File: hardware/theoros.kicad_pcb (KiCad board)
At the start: 4 copper layers, 60 x 120 mm, 87 parts, among them J201 TYPE-C-31-M-12, J301 TC2030-NL, J401 U.FL, J501 DM3AT-SF-PEJM5, J502 FH12-30S-0.5SH(55), SW301 RESET, SW302 BOOT, SW303 EJECT, U201 USBLC6-2SC6, U202 AP7361C-33E, U301 ESP32-S3-WROOM-1-N8, U302 MCP120T-300I/TT, U401 SAM-M10Q, U402 RFM95W-868S2, U501 TLV75801PDBV

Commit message: Rename project to Theoros and add V1.0 silkscreen artwork
Theoros (Greek θεωρός): an official observer and envoy, sent to watch
and report back.

Rename gps-lora to theoros everywhere: KiCad project, symbol and
footprint libraries, firmware library (theoros-core), umbrella header,
PC tool (tools/theoros.py), NVS namespaces, mDNS hostname, docs and
title blocks. The HKDF salt is now "theoros" (7 bytes), so every derived
key changes; the SECURITY.md test vectors are recomputed and host tests
pass. Boards provisioned with the old salt need re-provisioning.

Board revision is now V1.0. Silkscreen additions:
- Top: "THEOROS ${REVISION}" and "ΘΕΩΡΟΣ", an antenna warning next to
  J401, and a hidden line under the OLED panel.
- Bottom: an owl made as a solder-mask opening over the GND pour (gold
  with ENIG; vias inside stay tented) and the motto "ΟΡΩ ΚΑΙ ΑΓΓΕΛΛΩ /
  I SEE AND I REPORT".
Fab notes now state silkscreen on both sides and the intentional mask
opening. DRC is unchanged from before (4 silk-edge warnings).

Co-Authored-By: Claude Opus 5.5 <noreply@anthropic.com>
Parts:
- U301: footprint gps-lora:ESP32-S3-WROOM-1 -> theoros:ESP32-S3-WROOM-1
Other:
- board text added: "ANTENNA BEFORE TX >"
- board text added: "I SEE AND I REPORT"
- board text added: "THEOROS ${REVISION}"
- board text added: "WHO WATCHES THE WATCHER?"
- board text added: "YOU, APPARENTLY."
- board text added: "ΘΕΩΡΟΣ"
- board text added: "ΟΡΩ ΚΑΙ ΑΓΓΕΛΛΩ"

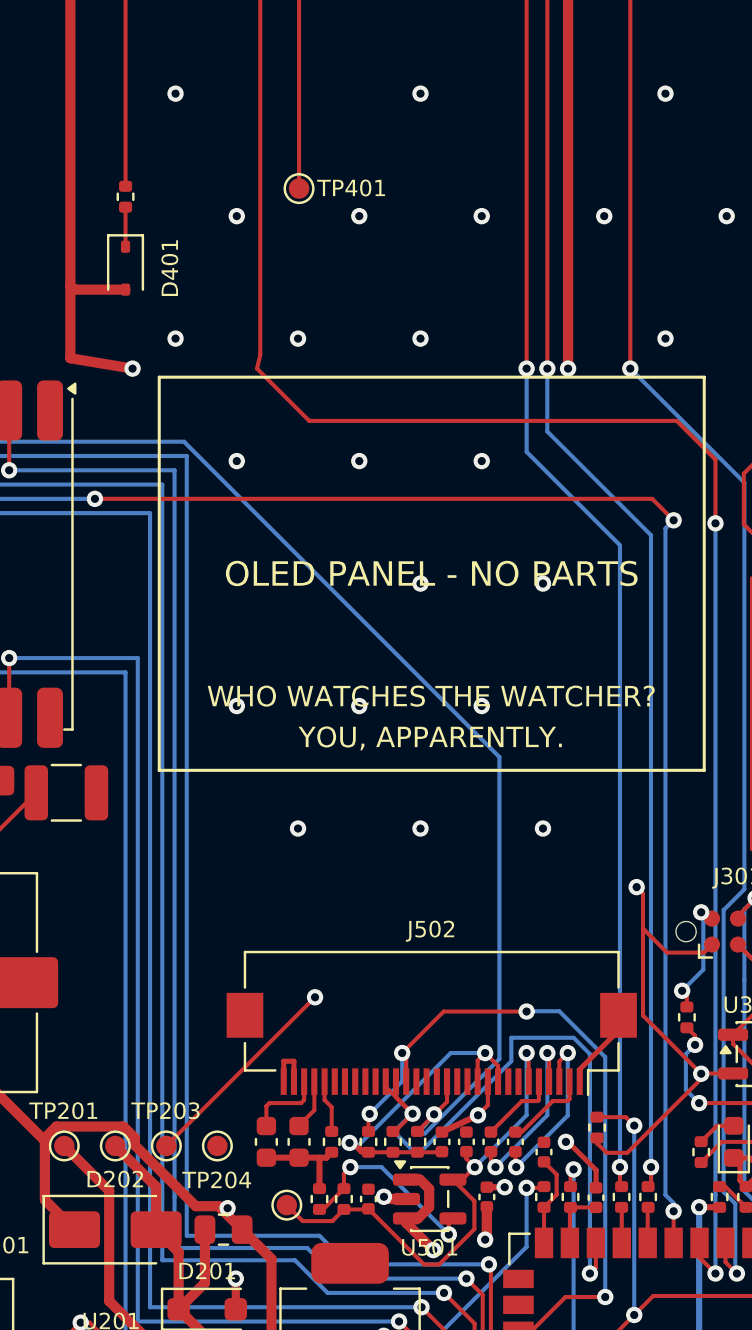
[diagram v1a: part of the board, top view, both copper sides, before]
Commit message: Fix J502 pin mapping, place C403 backup, check stackup impedance
J502: the panel FPC lands mirrored on the 180-degree FH12 (panel pin n on
J502 pin 31-n, per the ER-OLED0.96-1.1W drawing 1.4.1). The J502 symbol is
now mirrored in the schematic and the OLED support row is re-placed in the
new pin order and hand-routed. C305 (DNP) turns horizontal and R302 moves
0.4 mm east to make room.

C403: Seiko CPH3225A 11 mF chip EDLC on V_BCKP (~10 min hot-start
hold-up), with a new footprint from the Seiko drawing (pad 1 = +). D401
and R401, which charge it from 3V3, are now fitted. The unused Elna
footprint is removed.

Stackup: Lion's standard 4-layer 1.6 mm build (2116, 0.12 mm to L2) gives
47-49 ohm on LORA_ANT and 89-100 ohm on the USB pair with the existing
0.2 mm traces, so no impedance-controlled order is needed.

DRC: same 4 silk-edge warnings as before, 0 unconnected, schematic parity
clean. ERC clean.

Co-Authored-By: Claude Opus 5.5 <noreply@anthropic.com>
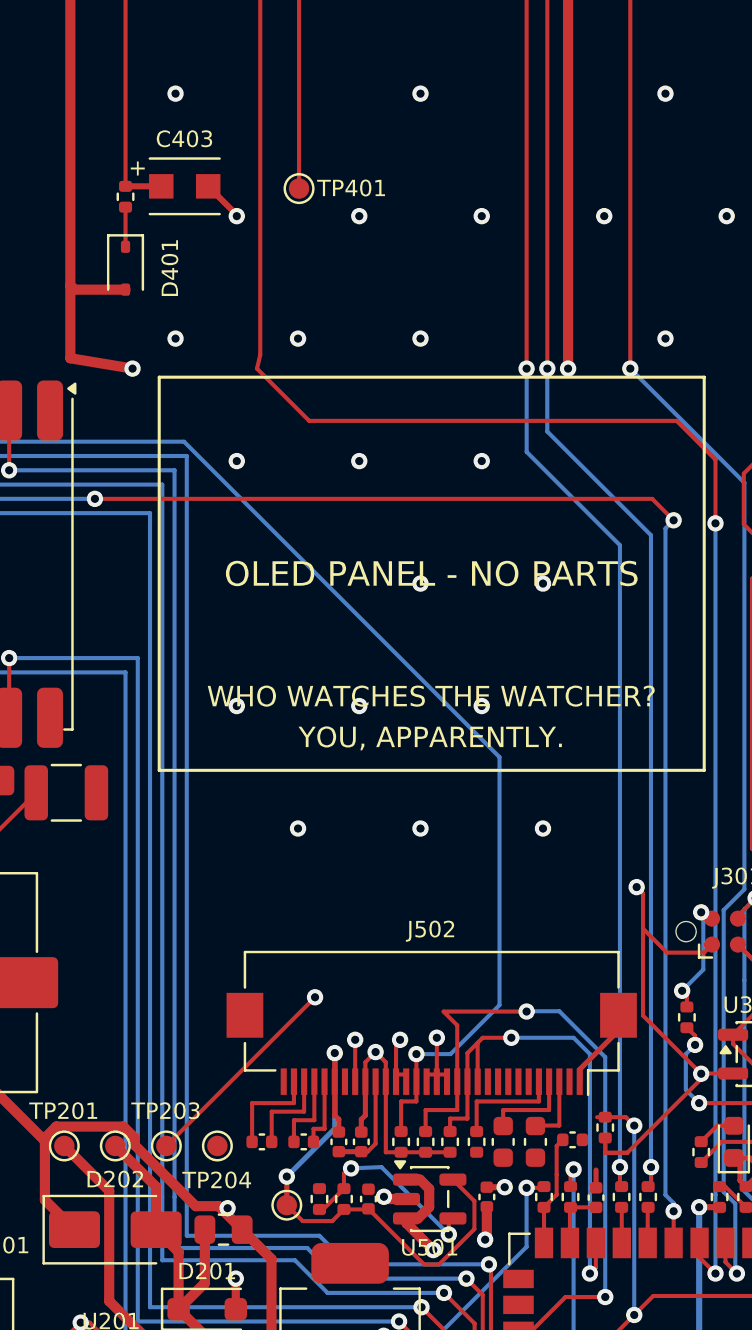
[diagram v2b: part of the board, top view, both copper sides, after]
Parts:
- added C403: 11mF 3.3V, theoros:Seiko_CPH3225A, F.Cu at (74.4, 79.5)
- moved C508 13.2 mm to (91.6, 126.3)
- moved C504 12.4 mm to (78.2, 126.3), turned to 180 degrees
- moved C509 10.0 mm to (90.0, 126.3)
- moved C505 9.17 mm to (80.2, 126.3), turned to 0 degrees
- moved R508 7.10 mm to (88.7, 126.3)
- moved C506 6.25 mm to (82.0, 126.3), turned to -90 degrees
- moved C507 3.95 mm to (83.0, 126.3), turned to -90 degrees
- moved R506 2.80 mm to (87.4, 126.3)
- moved R507 2.80 mm to (86.2, 126.3)
- moved C305 1.52 mm to (93.4, 126.2), turned to 0 degrees
- moved R505 0.80 mm to (85.0, 126.3)
- moved R302 0.40 mm to (95.0, 125.6)
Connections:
- J502 pad 11: +3V3 -> OLED_SDA
- J502 pad 12: GND -> OLED_SDA
- J502 pad 13: GND -> OLED_SCL
- J502 pad 14: OLED_RES -> GND
- J502 pad 17: GND -> OLED_RES
- J502 pad 18: OLED_SCL -> GND
- J502 pad 19: OLED_SDA -> GND
- J502 pad 2: /Storage & Display/OLED_C2N -> GND
- J502 pad 20: OLED_SDA -> +3V3
- J502 pad 22: GND -> +3V3
- J502 pad 24: GND -> unconnected-(J502-Pin_24-Pad24)
- J502 pad 25: GND -> /Storage & Display/OLED_VBAT
- J502 pad 26: /Storage & Display/OLED_IREF -> /Storage & Display/OLED_C1N
- J502 pad 27: /Storage & Display/OLED_VCOMH -> /Storage & Display/OLED_C1P
- J502 pad 28: /Storage & Display/OLED_VCC -> /Storage & Display/OLED_C2P
- J502 pad 29: GND -> /Storage & Display/OLED_C2N
- J502 pad 3: /Storage & Display/OLED_C2P -> /Storage & Display/OLED_VCC
- J502 pad 4: /Storage & Display/OLED_C1P -> /Storage & Display/OLED_VCOMH
- J502 pad 5: /Storage & Display/OLED_C1N -> /Storage & Display/OLED_IREF
- J502 pad 6: /Storage & Display/OLED_VBAT -> GND
- J502 pad 7: unconnected-(J502-Pin_7-Pad7) -> GND
- J502 pad 9: +3V3 -> GND
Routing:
- net OLED_SDA: track 32.5 -> 25.6 mm
- net /Storage & Display/OLED_C1P: track 8.93 -> 3.95 mm, vias 2 -> 0
- net /Storage & Display/OLED_C2P: track 8.98 -> 4.54 mm, vias 2 -> 0
- net +3V3: track 201.2 -> 197.3 mm, vias 14 -> 13
- net /Storage & Display/OLED_IREF: track 2.58 -> 5.49 mm
- net OLED_RES: track 165.7 -> 162.9 mm
- net /Storage & Display/OLED_VBAT: track 24.8 -> 27.3 mm
- net /Storage & Display/OLED_VCOMH: track 2.11 -> 4.43 mm
- net /Radio/GNSS_VBCKP: track 21.6 -> 23.3 mm
- net GND: track 44.5 -> 46.2 mm, vias 144 -> 145
- net OLED_SCL: track 34.4 -> 33.2 mm, vias 4 -> 2
- net /MCU/IO20_DP: track 4.48 -> 5.43 mm
- net /Storage & Display/OLED_C2N: track 4.17 -> 5.00 mm

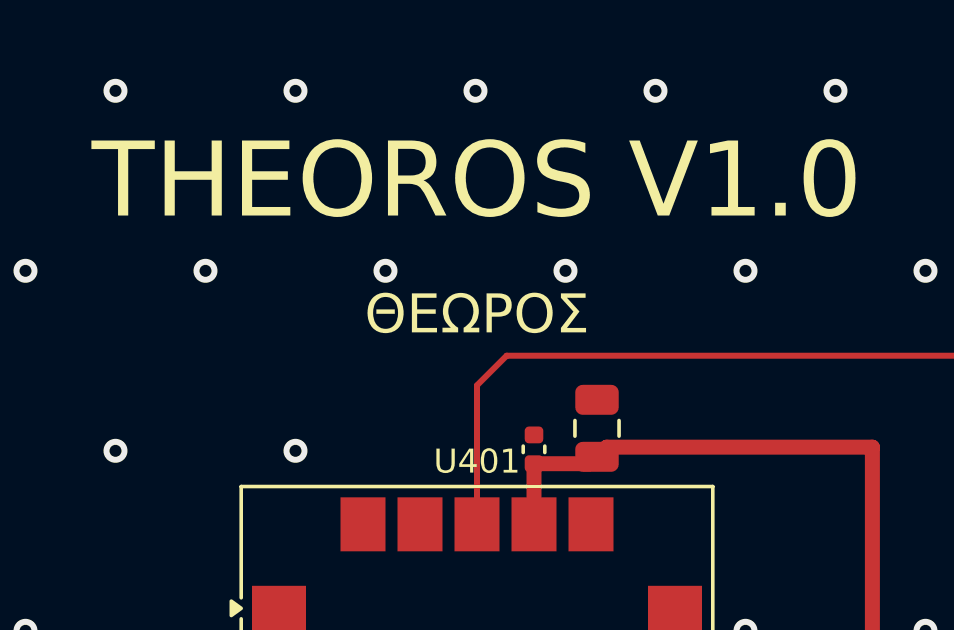
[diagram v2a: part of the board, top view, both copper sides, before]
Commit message: Replace Greek silkscreen text with Kannada
Top: ಥಿಯೋರೋಸ್ (Theoros in Kannada) under THEOROS ${REVISION}.
Bottom: motto ನೋಡುವೆ, ವರದಿ ಮಾಡುವೆ ("I see, I report") above the
English line, enlarged to 2 mm and both lines moved down slightly.

Both use Noto Sans Kannada Bold; KiCad keeps the shaped outlines in the
board file (render_cache), so they plot the same without the font
installed. ತಿಳಿಸುವೆ was avoided because its ಳಿ glyph fails the silkscreen
stroke check at any size. DRC unchanged: 4 silk-edge warnings, 0
unconnected, parity clean. README renders and PCB_DESIGN.md updated.

Co-Authored-By: Claude Opus 5.5 <noreply@anthropic.com>
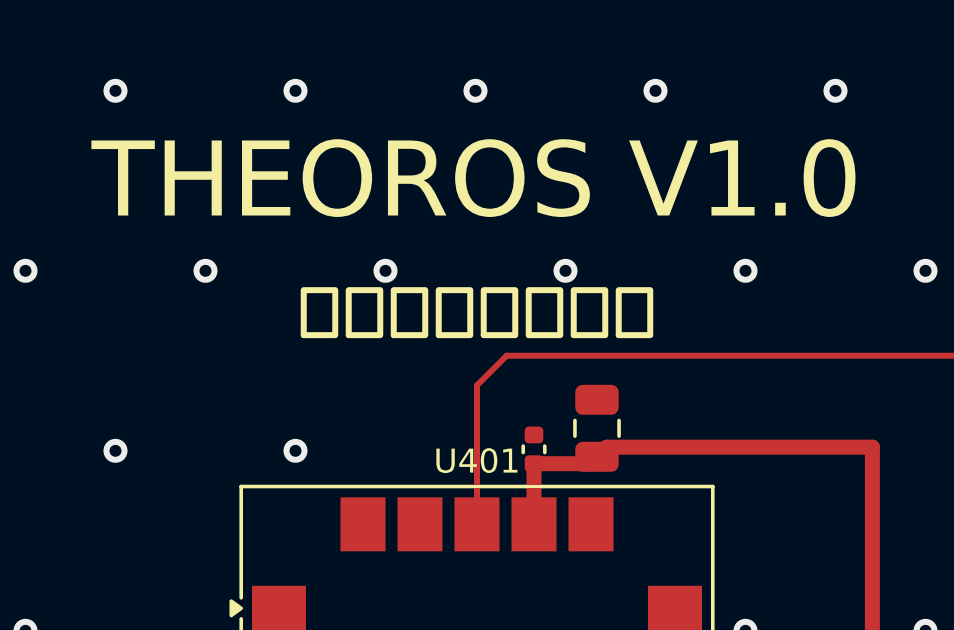
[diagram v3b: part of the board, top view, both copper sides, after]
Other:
- board text added: "ಥಿಯೋರೋಸ್"
- board text added: "ನೋಡುವೆ, ವರದಿ ಮಾಡುವೆ"
- board text removed: "ΘΕΩΡΟΣ"
- board text removed: "ΟΡΩ ΚΑΙ ΑΓΓΕΛΛΩ"
